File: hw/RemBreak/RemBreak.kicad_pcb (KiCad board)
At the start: 11 copper layers, 25 x 96 mm, 80 parts, among them IC1 LTC2943IDD#TRPBF, J1 Conn_01x03, J10 Screw_Terminal_01x02, J11 Conn_01x03, J12 Conn_01x01, J14 Conn_01x01, J2 Conn_02x06_Odd_Even, J4 Conn_01x07, J8 Conn_01x07, J9 Conn_01x07, Q1 BC337, Q11 BC337, Q12 BC847, Q2 BC847, Q3 BC847, Q4 BC337, Q5 BC847, Q6 BC337, Q7 BC847, Q8 SiS415DNT, Q9 BC337, U1 L7805, U2 L7805, U3 XC6220B331MR, U4 MAX40200AUK, U6 INA219BxDCN, U7 MAX40200AUK, U8 BD48ExxG, U9 BD48ExxG

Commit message: updated pcb and schematics - still in progress
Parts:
- removed R3: 0R, Resistor_SMD:R_0805_2012Metric
- added J3: Screw_Terminal_01x04, TerminalBlock_Phoenix:TerminalBlock_Phoenix_MPT-0,5-4-2.54_1x04_P2.54mm_Horizontal, F.Cu at (69.5, 69.3)
- added J5: Screw_Terminal_01x04, TerminalBlock_Phoenix:TerminalBlock_Phoenix_MPT-0,5-4-2.54_1x04_P2.54mm_Horizontal, F.Cu at (69.5, 81.1)
- C1, C2, C3, C4, IC1, J12, J14, M1, Q12, Q2, Q3, Q5, Q7, Q8, R10, R11, R12, R13, R14, R15, R16, R17, R18, R19, R20, R21, R22, R23, R24, R25, R26, R27, R28, R29, R30, R31, R32, R33, R34, R35, R36, R37, R38, R39, R4, R40, R41, R42, R43, R44, R5, R6, R7, R8, R9, U3, U4, U6, U7, U8, U9: moved to B.Cu
- J1: moved to F.Cu
- J11: footprint Connector_JST:JST_XH_B3B-XH-A_1x03_P2.50mm_Vertical -> Connector_JST:JST_XH_S3B-XH-SM4-TB_1x03-1MP_P2.50mm_Horizontal
- J2: footprint Connector_PinHeader_2.54mm:PinHeader_2x06_P2.54mm_Vertical_SMD -> dodo_conn:SAMTEC_TSM-106-01-L-DH-P-TR
- J4, J8, J9: footprint Connector_PinSocket_2.54mm:PinSocket_1x07_P2.54mm_Vertical -> Connector_PinSocket_2.54mm:PinSocket_1x07_P2.54mm_Vertical_SMD_Pin1Left
- U2: footprint Package_TO_SOT_THT:TO-220-3_Horizontal_TabDown -> Package_TO_SOT_THT:TO-220-3_Vertical
- moved R1 148.3 mm to (34.1, 44.0)
- moved R2 148.3 mm to (34.1, 47.0)
- moved U1 125.3 mm to (57.6, 37.5), turned to 180 degrees
- moved Q8 120.4 mm to (51.6, 23.5), turned to 180 degrees
- moved IC1 107.9 mm to (57.0, 23.2)
- moved Q11 97.5 mm to (106.4, 75.3), turned to 90 degrees
- moved Q1 97.3 mm to (104.5, 65.5)
- moved Q6 91.6 mm to (110.5, 65.5)
- moved Q9 88.0 mm to (116.2, 65.5)
- moved J10 87.9 mm to (70.0, 25.2), turned to 180 degrees
- moved R15 87.4 mm to (58.0, 29.0), turned to 180 degrees
- moved J4 86.9 mm to (51.6, 106.5)
- moved J11 86.4 mm to (55.0, 26.0), turned to 180 degrees
- moved U2 85.3 mm to (71.4, 40.0), turned to 90 degrees
- moved Q4 78.7 mm to (122.2, 65.5)
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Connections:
- C1 pad 1: /power_switch/7V4 -> Net-(J12-Pin_1)
- J2 pad 10: unconnected-(J2-Pin_10-Pad10) -> /SCL
- J2 pad 11: unconnected-(J2-Pin_11-Pad11) -> GND
- J2 pad 12: unconnected-(J2-Pin_12-Pad12) -> GND
- R1 pad 1: unconnected-(R1-Pad1) -> /7V5
- R1 pad 2: unconnected-(R1-Pad2) -> Net-(J3-Pin_1)
- R2 pad 1: Net-(R2-Pad1) -> /VEXT
- R2 pad 2: unconnected-(R2-Pad2) -> Net-(J3-Pin_1)
- U1 pad 1: /power_switch/7V4 -> Net-(J12-Pin_1)
- U2 pad 1: /power_switch/7V4 -> Net-(J12-Pin_1)

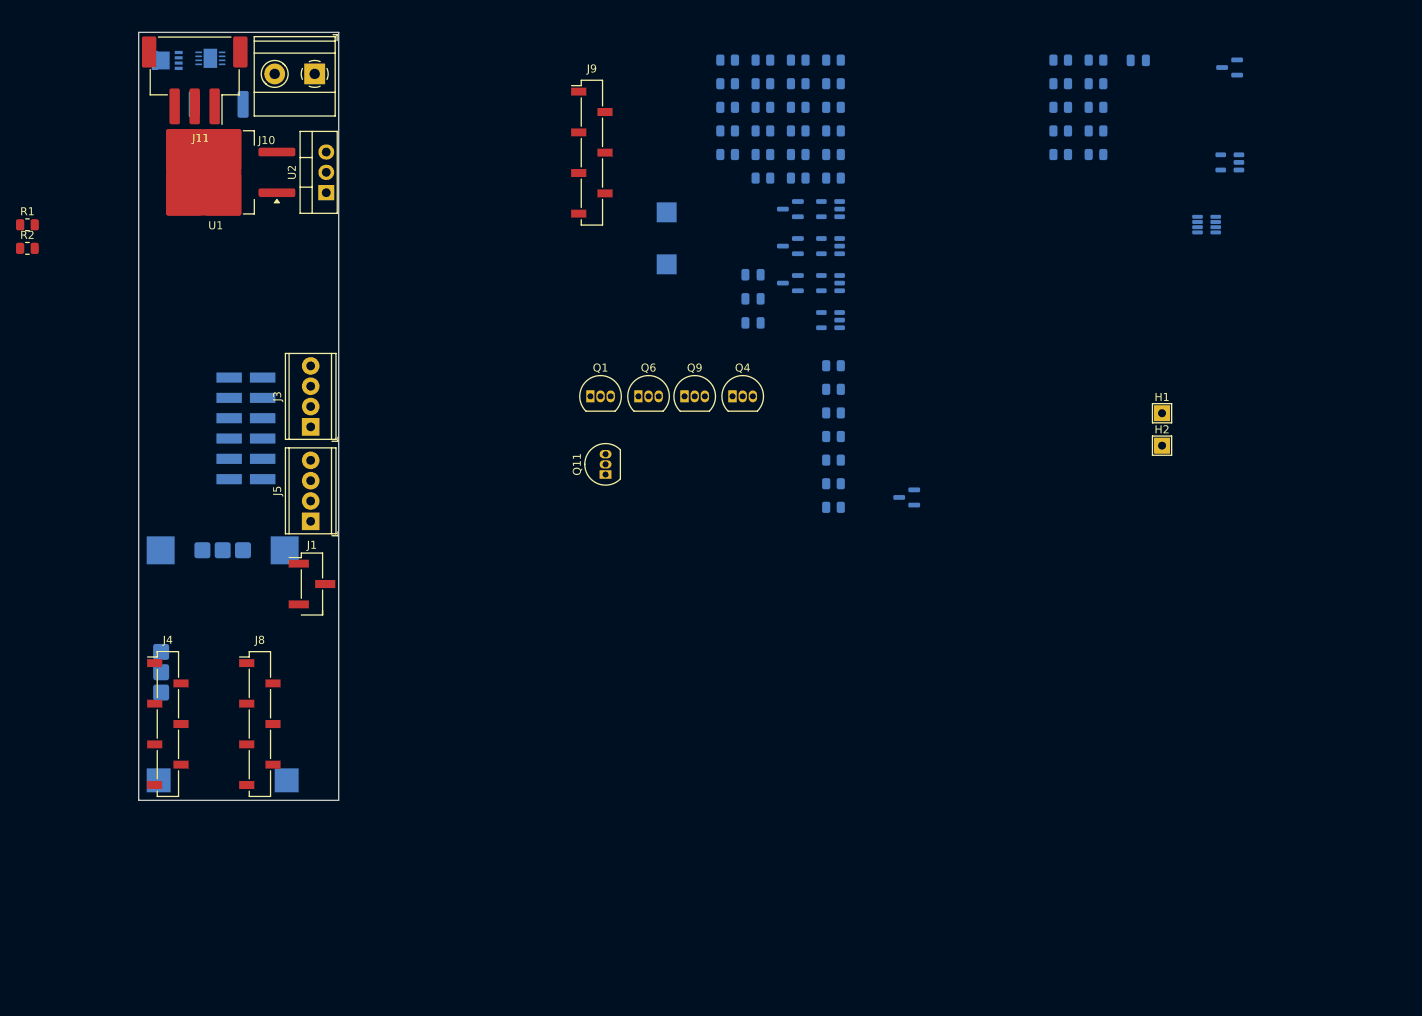
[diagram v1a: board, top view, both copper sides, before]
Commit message: changed size of the board and development of schematic
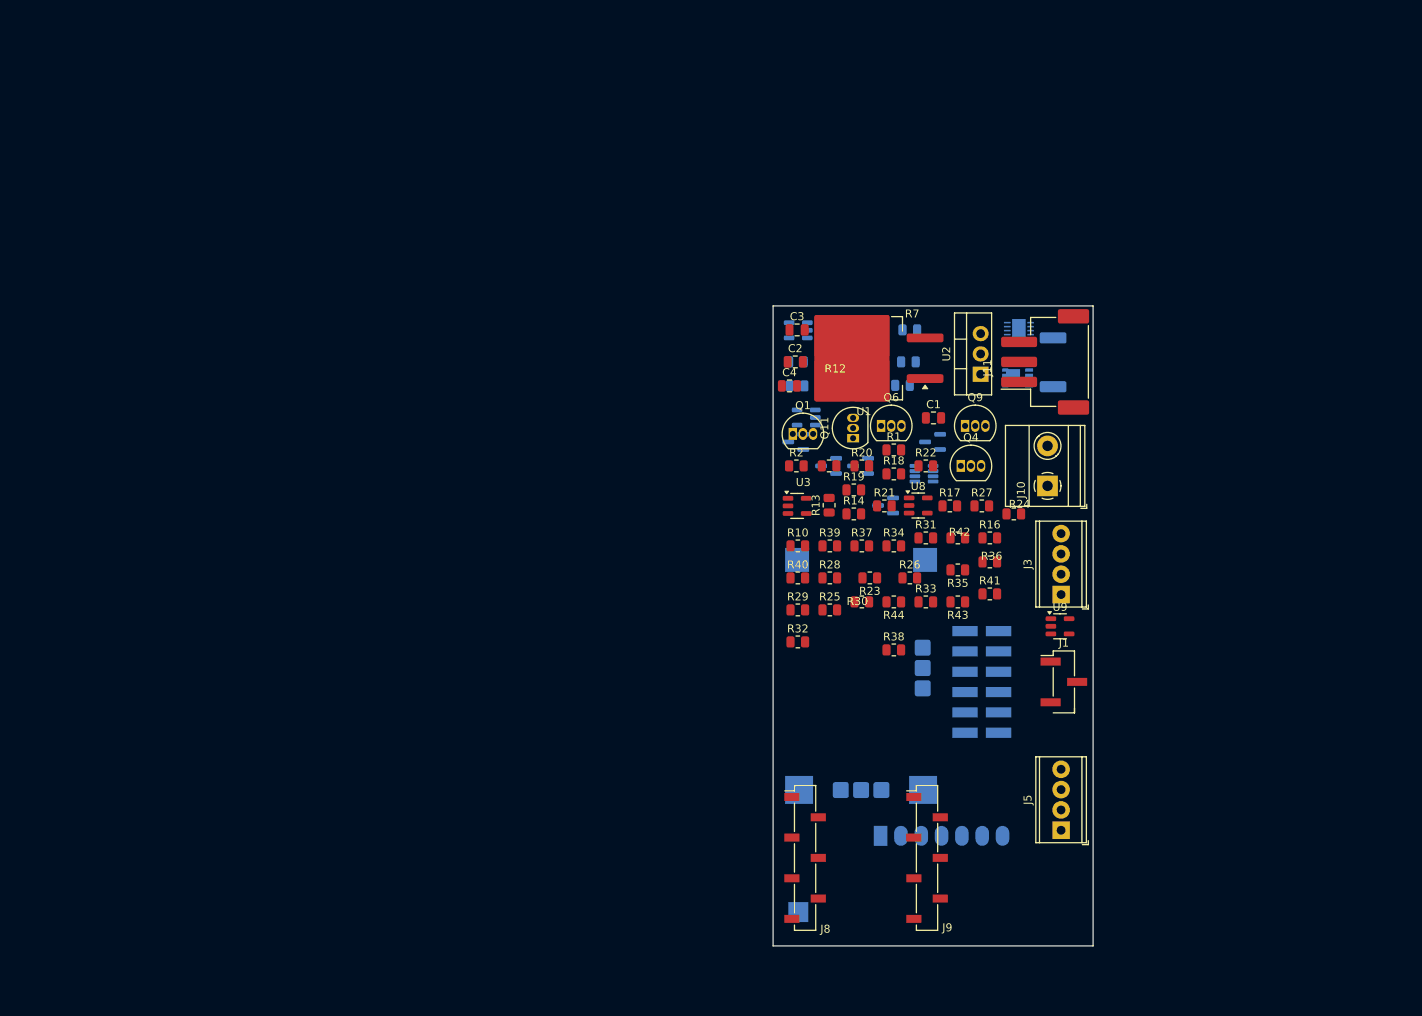
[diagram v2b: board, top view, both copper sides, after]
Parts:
- removed H1, H2: MountingHole_Pad, TestPoint:TestPoint_THTPad_2.0x2.0mm_Drill1.0mm
- removed J12, J14: Conn_01x01, TestPoint:TestPoint_Pad_2.5x2.5mm
- removed J4: Conn_01x07, Connector_PinSocket_2.54mm:PinSocket_1x07_P2.54mm_Vertical_SMD_Pin1Left
- added M2: ~, chinese_modules:RF_controller, B.Cu at (143.1, 125.3)
- C1, C2, C3, C4, R10, R12, R13, R14, R16, R17, R18, R19, R20, R21, R22, R23, R24, R25, R26, R27, R28, R29, R30, R31, R32, R33, R34, R35, R36, R37, R38, R39, R40, R41, R42, R43, R44, U3, U8, U9: moved to F.Cu
- moved Q8 113.5 mm to (157.9, 63.2)
- moved J11 112.0 mm to (161.3, 61.2), turned to 90 degrees
- moved R1 111.9 mm to (142.4, 72.2)
- moved J2 109.5 mm to (159.8, 101.2), turned to 90 degrees
- moved R15 109.2 mm to (162.3, 61.2), turned to -90 degrees
- moved IC1 106.6 mm to (158.0, 57.0)
- moved J10 105.1 mm to (161.6, 76.7), turned to 90 degrees
- moved J5 101.4 mm to (163.3, 119.7)
- moved R2 99.9 mm to (130.2, 74.2)
- moved J9 97.6 mm to (146.5, 123.2)
- moved J3 96.1 mm to (163.3, 90.3)
- moved J1 94.8 mm to (163.6, 101.2)
- moved U2 84.9 mm to (153.2, 62.7)
- moved U1 84.3 mm to (138.7, 60.7)
- moved M1 79.8 mm to (138.3, 100.4), turned to -90 degrees
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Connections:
- net Net-(J12-Pin_1) renamed /power_switch/SW-
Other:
- board size 25 x 96 mm -> 40 x 80 mm
- board text added: "3 (5)mm odstpu od kraju"
- board text removed: "Dodat Pavlovi sirenu a LEDku STEP"
- board text removed: "LED indikator externi THT"
- board text removed: "USB C uplne dolu do kraje"
- board text removed: "sirena jako externi"
- board text removed: "sroubovaci terminal na konektor na handlebar"

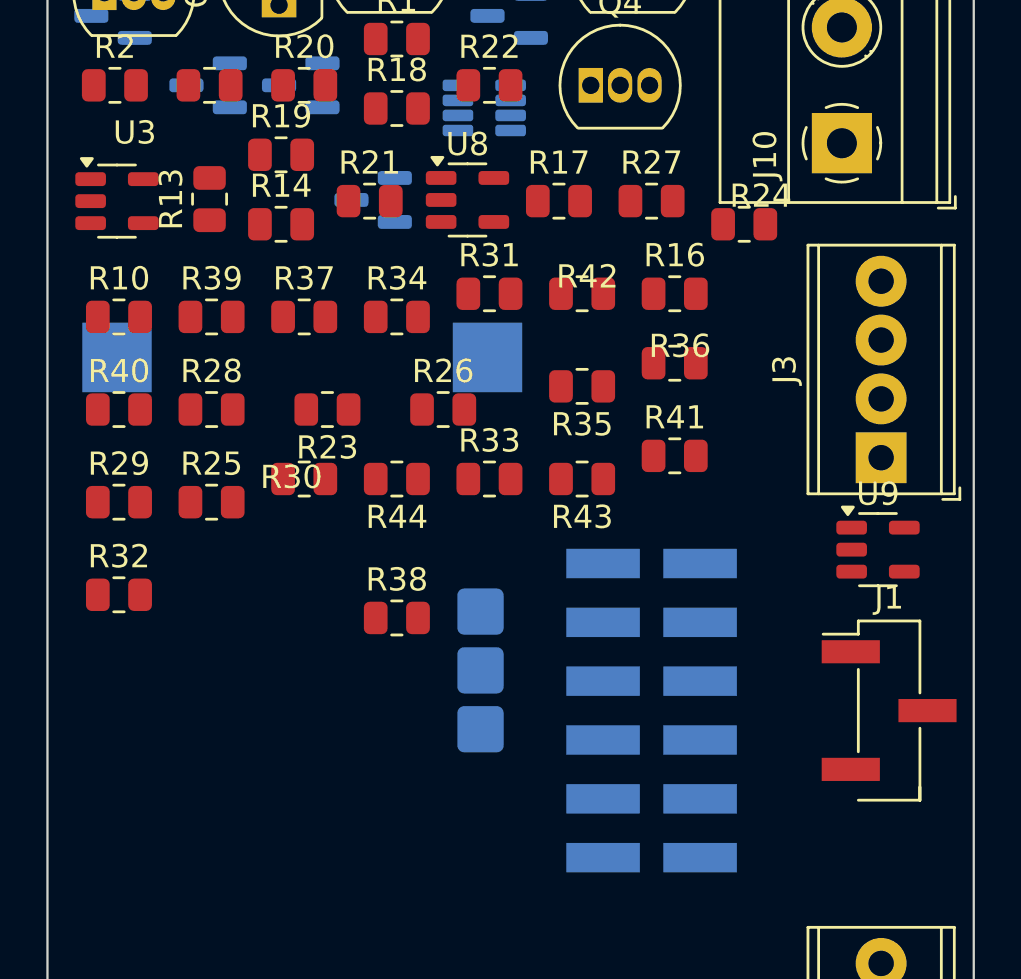
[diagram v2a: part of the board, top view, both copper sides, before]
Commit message: added RGB LED connection - missing connections in schematics
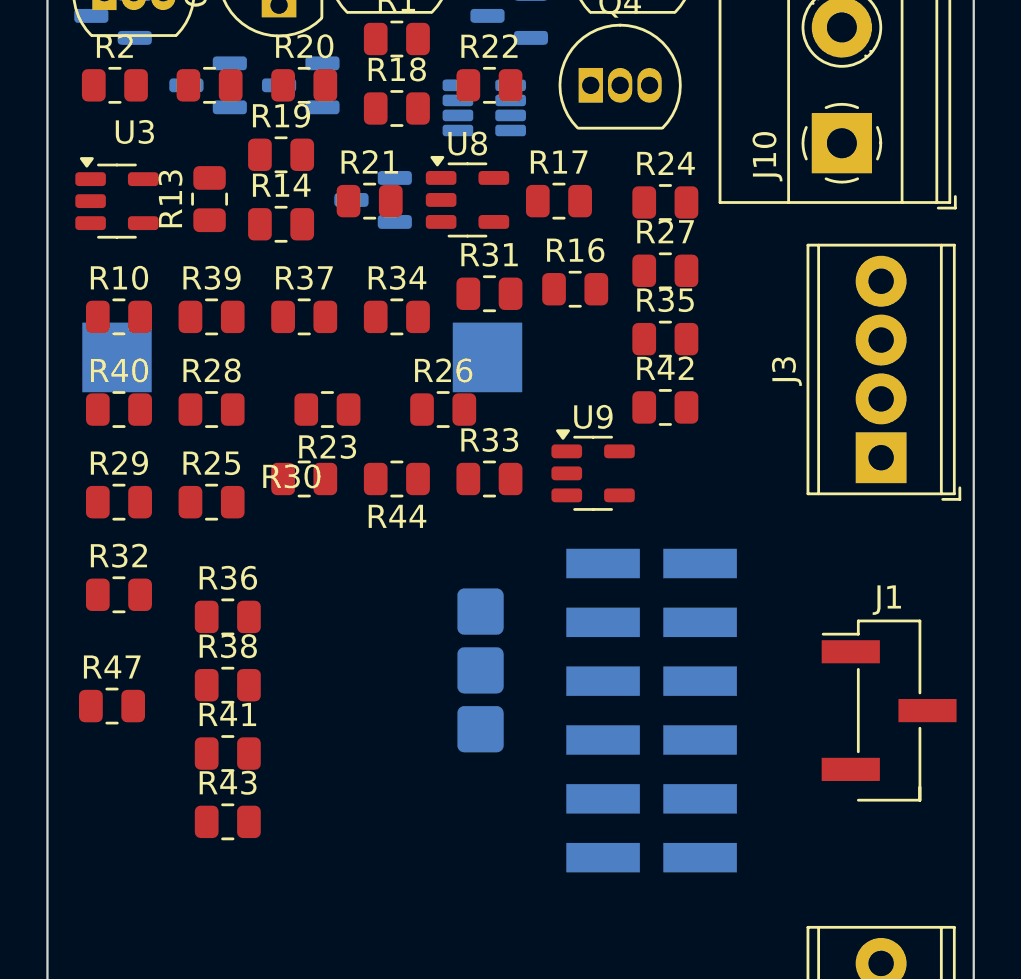
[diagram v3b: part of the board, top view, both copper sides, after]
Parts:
- added R47: 4k2, Resistor_SMD:R_0805_2012Metric, F.Cu at (130.1, 101.0)
- moved R41 23.2 mm to (135.1, 103.0)
- moved R36 22.2 mm to (135.1, 97.2)
- moved R43 21.3 mm to (135.1, 106.0), turned to 0 degrees
- moved U9 12.7 mm to (150.9, 91.0)
- moved R38 7.86 mm to (135.1, 100.1)
- moved R42 6.09 mm to (154.0, 88.1)
- moved R16 4.30 mm to (150.1, 83.0)
- moved R35 4.13 mm to (154.0, 85.2), turned to 0 degrees
- moved R24 3.53 mm to (154.0, 79.3)
- moved R27 3.07 mm to (154.0, 82.2)
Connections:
- net Net-(M1-LED) renamed /power_manager/CHARGED
- net Net-(Q3-C) renamed /power_switch/RUNNIG
- J2 pad 10: /SCL -> GND
- J2 pad 11: GND -> /SDA
- J2 pad 12: GND -> /SCL
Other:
- board text added: "- 3 (5)mm odstpu od kraju"
- board text added: "- Connect schematics, check if the power symbols connect components across the whole schematics - connect missig wires to MCU and the 12pin connector"
- board text removed: "3 (5)mm odstpu od kraju"

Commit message: finished schematics routing and erc passed
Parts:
- removed U6: INA219BxDCN, Package_TO_SOT_SMD:SOT-23-8
- added U5: INA219BxDCN, Package_TO_SOT_SMD:SOT-23-8, B.Cu at (146.0, 75.0)
- IC1: footprint Package_DFN_QFN:DFN-8-1EP_3x3mm_P0.5mm_EP1.7x2.4mm -> Package_DFN_QFN:DFN-8-1EP_3x3mm_P0.5mm_EP1.66x2.38mm
- J2: footprint dodo_conn:SAMTEC_TSM-106-01-L-DH-P-TR -> chinese_modules:SAMTEC_TSM-106-01-L-DH-P-TR
- moved J2 0.33 mm to (159.5, 101.3)
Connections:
- net /break_control/Display_DCKI renamed /break_control/DISPLAY.DCKI
- net /break_control/Display_DI renamed /break_control/DISPLAY.DI
- net /power_manager/CHARGED renamed /power_manager/CHARGED (GREEN)
- net /power_switch/RUNNIG renamed /power_switch/RUNNIG (RED)
- net /power_switch/SW- renamed /power_switch/ON/OFF
- net Button_RF renamed Net-(J8-Pin_2)
- C2 pad 1: /power_switch/5V -> +5V
- IC1 pad 4: unconnected-(IC1-SCL-Pad4) -> /break_control/I2C.SCL
- IC1 pad 5: unconnected-(IC1-SDA-Pad5) -> /break_control/I2C.SDA
- IC1 pad 6: /power_manager/BALARM -> /break_control/BALARM
- J1 pad 1: /break_control/7V4 -> +7.5V
- J2 pad 11: /SDA -> /break_control/I2C.SDA
- J2 pad 12: /SCL -> /break_control/I2C.SCL
- J3 pad 2: /BUZZER -> /break_control/BUZZER
- J3 pad 3: /BUTTON -> /break_control/BUTTON
- J5 pad 1: /7V5 -> +7.5V
- J8 pad 5: /break_control/SDA -> /break_control/I2C.SDA
- J8 pad 6: /break_control/SCL -> /break_control/I2C.SCL
- J9 pad 5: /break_control/3V3 -> +3V3
- M2 pad 2: /break_control/5V -> +5V
- Q4 pad 1: /power_manager/CHARGING -> /break_control/CHARGING
- Q5 pad 3: /power_manager/CHARGING -> /break_control/CHARGING
- Q8 pad 5: /power_switch/7V4 -> +7.5V
- R1 pad 1: /7V5 -> +7.5V
- R10 pad 2: /power_switch/5V -> +5V
- R11 pad 1: /break_control/3V3 -> +3V3
- R12 pad 2: unconnected-(R12-Pad2) -> /break_control/I2C.SDA
- R13 pad 2: unconnected-(R13-Pad2) -> /break_control/I2C.SCL
- R19 pad 2: /power_manager/CHARGING -> /break_control/CHARGING
- R22 pad 2: /power_manager/BALARM -> /break_control/BALARM
- U1 pad 3: /power_switch/5V -> +5V
- U2 pad 3: /power_switch/5V -> +5V
- U3 pad 1: /power_switch/5V -> +5V
- U4 pad 5: /power_switch/3V3 -> +3V3
- U7 pad 1: /power_manager/VBUS -> /break_control/VBUS

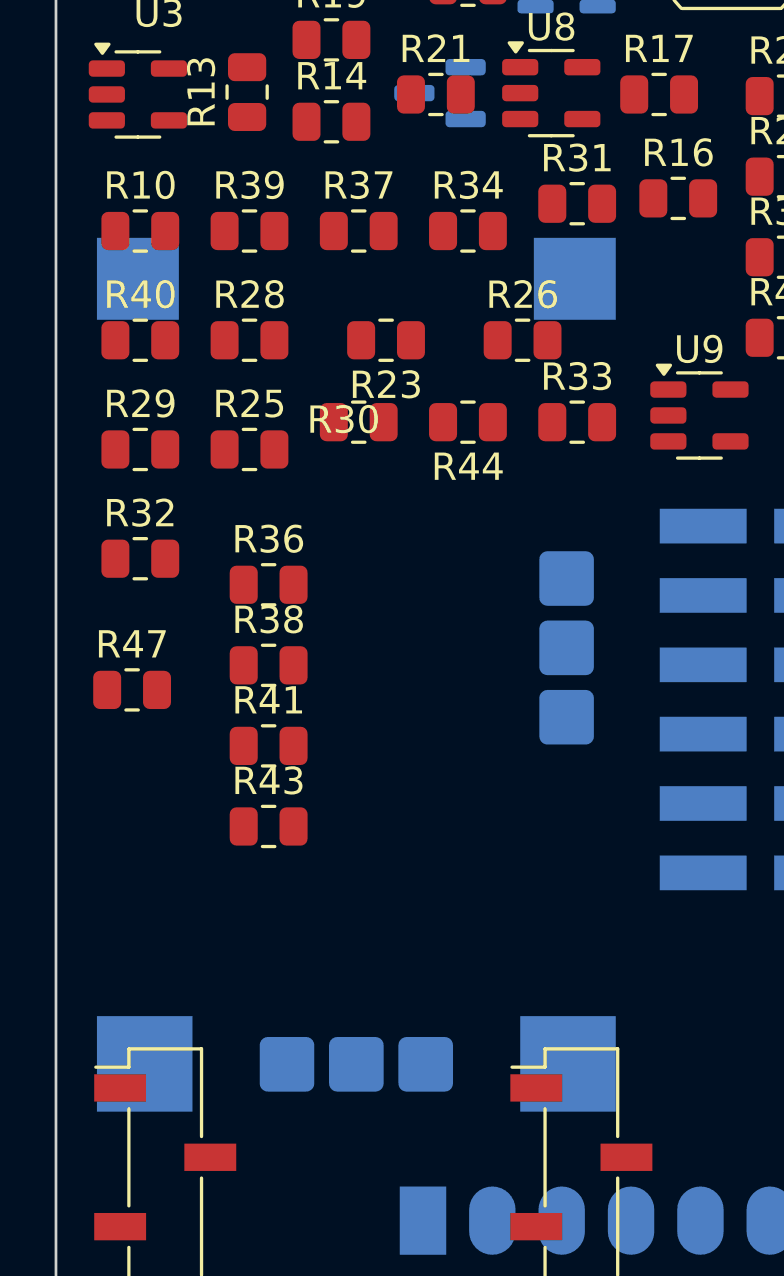
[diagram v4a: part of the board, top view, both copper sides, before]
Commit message: fixed errors in schematics
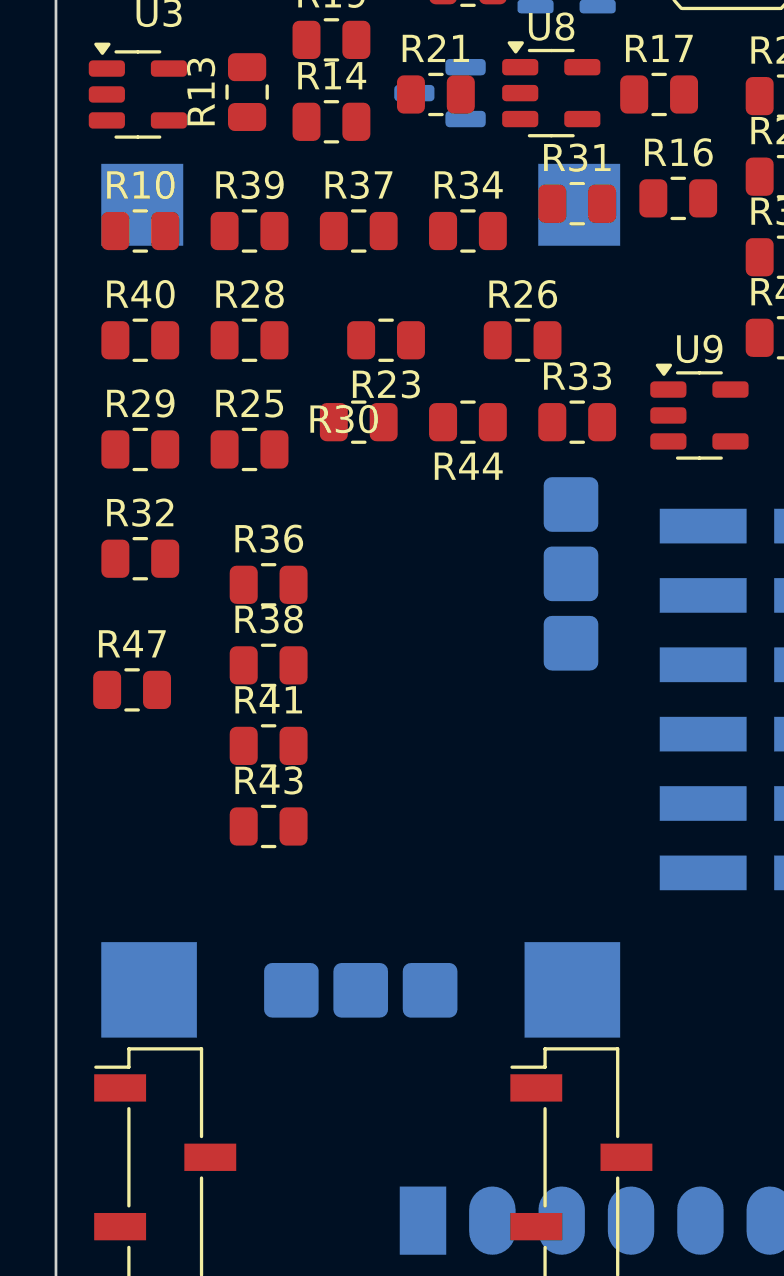
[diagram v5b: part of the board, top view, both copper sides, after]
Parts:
- moved M1 2.71 mm to (138.5, 97.7)
